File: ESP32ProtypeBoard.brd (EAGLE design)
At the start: 78.7 x 54.6 mm, 89 parts, among them IC1 ACT4088US-T, IC2 SI4431BDY, J4 VCC_TERMINAL, Q4 BSS138, U1 3.3V, U2 ESP-WROOM-32

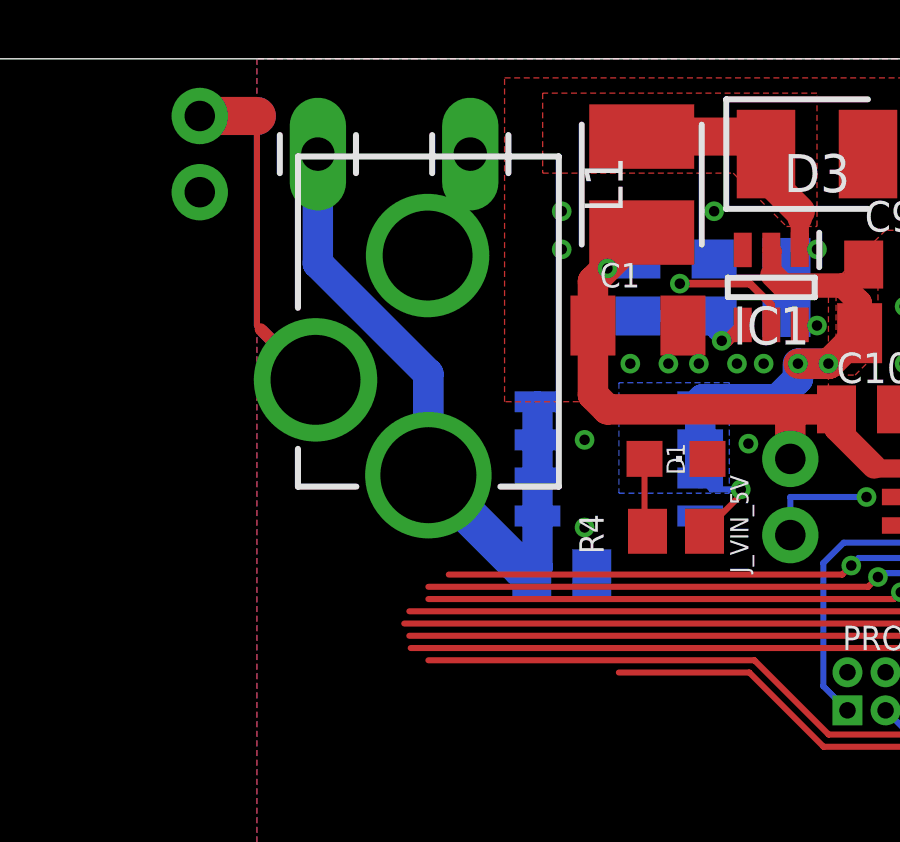
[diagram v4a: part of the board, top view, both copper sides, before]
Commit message: 12V pin
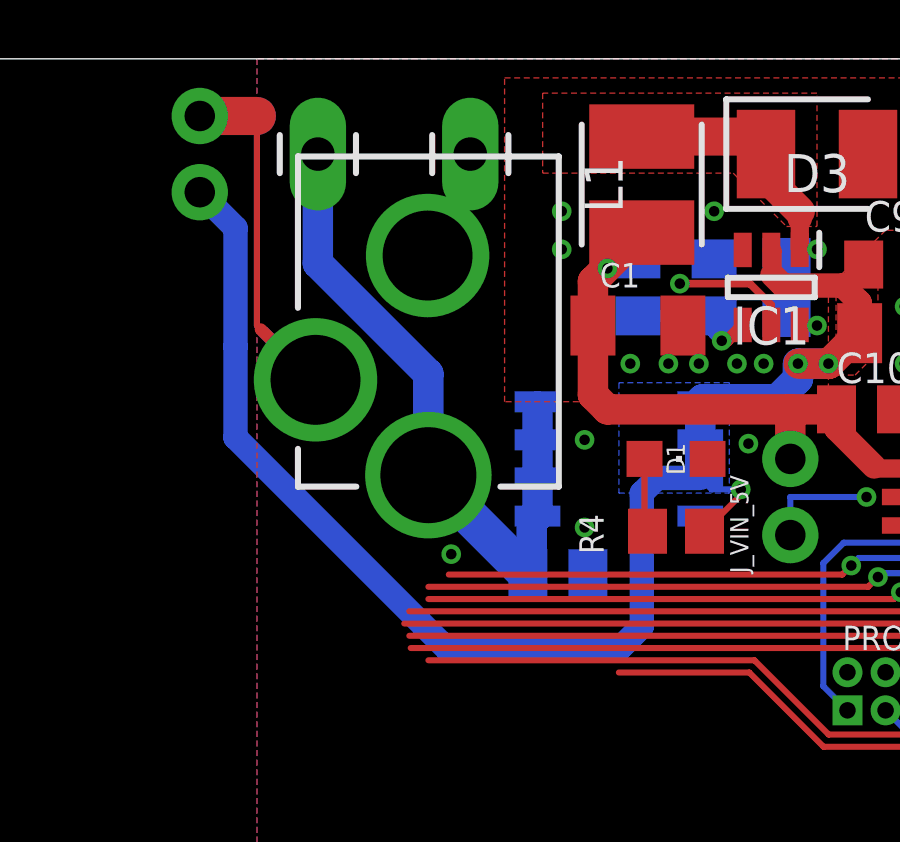
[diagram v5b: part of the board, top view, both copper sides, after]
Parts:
- moved C8 0.13 mm to (28.4, 37.5)
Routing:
- net +12V: track 18.6 -> 50.7 mm
- net GND: vias 31 -> 32
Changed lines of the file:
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@@
 <attribute name="VALUE" x="26.035" y="53.467" size="0.6096" layer="27" font="vector" ratio="20" rot="R180"/>
 </element>
-<element name="C8" library="rcl" library_urn="urn:adsk.eagle:library:334" package="C0805K" package3d_urn="urn:adsk.eagle:package:23681/2" value="0.1uF" x="28.575" y="37.465" smashed="yes" rot="MR180">
-<attribute name="NAME" x="29.21" y="38.735" size="0.8128" layer="26" rot="MR0"/>
-<attribute name="POPULARITY" value="52" x="28.575" y="37.465" size="1.778" layer="28" rot="MR180" display="off"/>
-<attribute name="SPICEPREFIX" value="C" x="28.575" y="37.465" size="1.778" layer="28" rot="MR180" display="off"/>
-<attribute name="VALUE" x="28.702" y="38.735" size="0.8128" layer="28" rot="MR0" align="bottom-center"/>
-<attribute name="VOLTAGE" value="25V" x="28.575" y="37.465" size="1.778" layer="28" rot="MR180" display="off"/>
+<element name="C8" library="rcl" library_urn="urn:adsk.eagle:library:334" package="C0805K" package3d_urn="urn:adsk.eagle:package:23681/2" value="0.1uF" x="28.448" y="37.465" smashed="yes" rot="MR180">
+<attribute name="NAME" x="29.083" y="38.735" size="0.8128" layer="26" rot="MR0"/>
+<attribute name="POPULARITY" value="52" x="28.448" y="37.465" size="1.778" layer="28" rot="MR180" display="off"/>
+<attribute name="SPICEPREFIX" value="C" x="28.448" y="37.465" size="1.778" layer="28" rot="MR180" display="off"/>
+<attribute name="VALUE" x="28.575" y="38.735" size="0.8128" layer="28" rot="MR0" align="bottom-center"/>
+<attribute name="VOLTAGE" value="25V" x="28.448" y="37.465" size="1.778" layer="28" rot="MR180" display="off"/>
 </element>
 <element name="J12" library="SparkFun-Connectors" library_urn="urn:adsk.eagle:library:513" package="1X11_NO_SILK" package3d_urn="urn:adsk.eagle:package:38260/1" value="" x="86.995" y="9.525" smashed="yes" rot="MR180">
@@
 <wire x1="36.195" y1="38.735" x2="36.195" y2="40.005" width="0.2032" layer="16"/>
 <wire x1="36.195" y1="40.005" x2="38.735" y2="40.005" width="0.2032" layer="16"/>
+<via x="24.892" y="38.1" extent="1-16" drill="0.35"/>
 <wire x1="125.095" y1="27.305" x2="130.175" y2="42.799" width="0" layer="19" extent="1-1"/>
 <wire x1="104.14" y1="29.21" x2="125.095" y2="27.305" width="0" layer="19" extent="1-1"/>
@@
 <wire x1="34.544" y1="40.259" x2="33.573" y2="40.259" width="0.2032" layer="16"/>
 <wire x1="33.573" y1="40.259" x2="33.192" y2="40.64" width="0.2032" layer="16"/>
-<wire x1="33.192" y1="43.18" x2="16.51" y2="50.165" width="0" layer="19" extent="16-16"/>
-<wire x1="36.4734" y1="44.45" x2="36.449" y2="44.45" width="0" layer="19" extent="1-1"/>
+<wire x1="33.192" y1="40.64" x2="31.75" y2="40.64" width="0.8128" layer="16"/>
+<wire x1="31.75" y1="40.64" x2="31.242" y2="40.132" width="0.8128" layer="16"/>
+<wire x1="31.242" y1="35.687" x2="30.48" y2="34.925" width="0.8128" layer="16"/>
+<wire x1="17.6996" y1="45.01545625" x2="17.702" y2="45.01785625" width="0.8128" layer="16"/>
+<wire x1="17.6996" y1="41.9904" x2="17.6996" y2="45.01545625" width="0.8128" layer="16"/>
+<wire x1="17.702" y1="48.973" x2="16.51" y2="50.165" width="0.8128" layer="16"/>
+<wire x1="31.242" y1="40.132" x2="31.242" y2="35.687" width="0.8128" layer="16"/>
+<wire x1="30.48" y1="34.925" x2="24.765" y2="34.925" width="0.8128" layer="16"/>
+<wire x1="24.765" y1="34.925" x2="17.6996" y2="41.9904" width="0.8128" layer="16"/>
+<wire x1="17.702" y1="45.01785625" x2="17.702" y2="48.973" width="0.8128" layer="16"/>
+<wire x1="36.449" y1="44.45" x2="36.4734" y2="44.45" width="0" layer="19" extent="1-1"/>
 </signal>
 <signal name="+5V">
@@
 <wire x1="20.4452" y1="47.7944625" x2="24.13" y2="44.1096625" width="1.016" layer="16"/>
 <wire x1="24.13" y1="40.7322" x2="27.2702" y2="37.592" width="1.27" layer="16"/>
-<wire x1="27.448" y1="37.592" x2="27.575" y2="37.465" width="1.27" layer="16"/>
-<wire x1="27.448" y1="37.592" x2="27.2702" y2="37.592" width="1.27" layer="16"/>
 <wire x1="27.768" y1="42.799" x2="27.768" y2="43.18" width="0.7112" layer="16"/>
 <wire x1="27.768" y1="41.91" x2="27.768" y2="40.64" width="1.016" layer="16"/>
 <wire x1="27.768" y1="40.64" x2="27.768" y2="39.37" width="1.016" layer="16"/>
-<wire x1="27.768" y1="39.37" x2="27.768" y2="37.658" width="1.016" layer="16"/>
-<wire x1="27.768" y1="37.658" x2="27.575" y2="37.465" width="1.016" layer="16"/>
 <wire x1="27.768" y1="41.91" x2="27.768" y2="42.799" width="1.016" layer="16"/>
+<wire x1="27.575" y1="39.177" x2="27.575" y2="37.592" width="1.016" layer="16"/>
+<wire x1="27.448" y1="37.465" x2="27.575" y2="37.592" width="1.016" layer="16"/>
+<wire x1="27.575" y1="39.177" x2="27.768" y2="39.37" width="1.016" layer="16"/>
+<wire x1="27.448" y1="37.465" x2="27.2702" y2="37.592" width="0" layer="19" extent="16-16"/>
 </signal>
 <signal name="D2A">

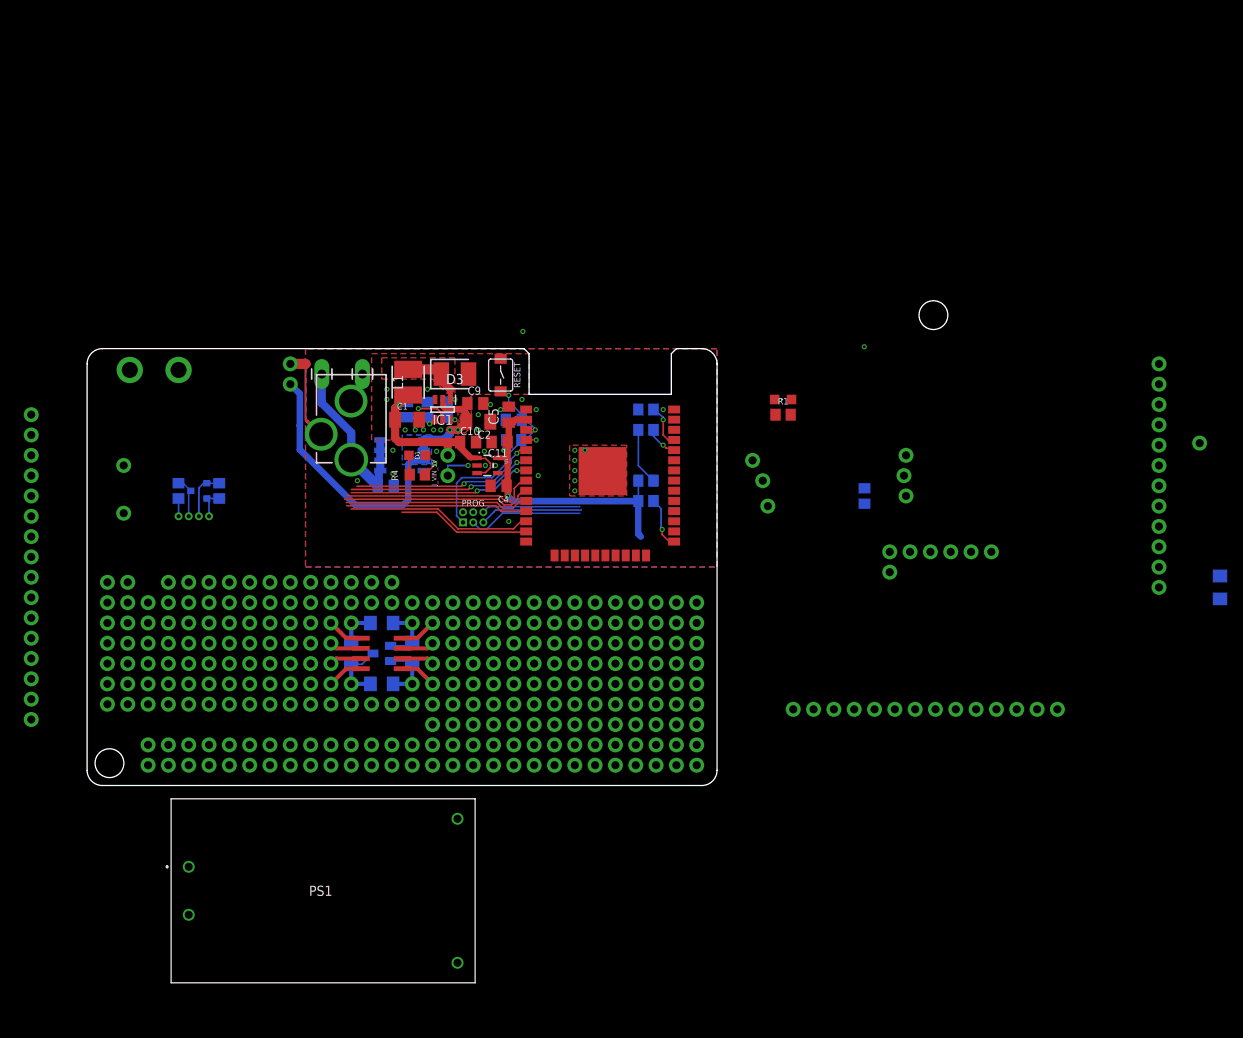
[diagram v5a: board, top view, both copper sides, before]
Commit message: first data lines, added new VIN pin closer
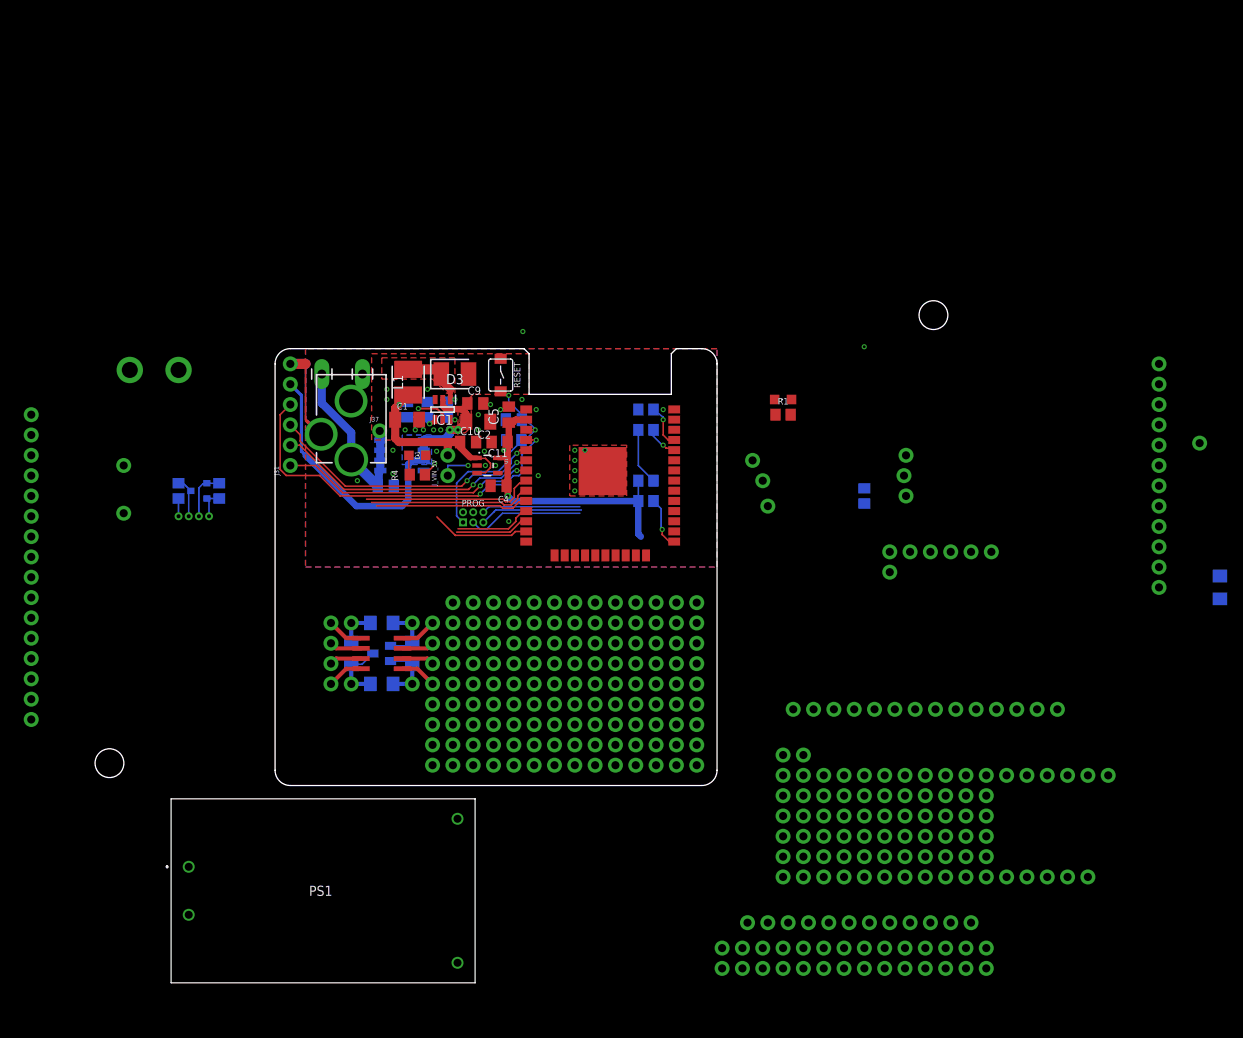
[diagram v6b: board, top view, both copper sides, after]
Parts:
- added J31: (no value), SparkFun-Connectors:1X04_NO_SILK
- added J37: (no value), SparkFun-Connectors:1X01NS_KIT
- moved J1 87.2 mm to (78.1, -8.89)
- moved J13 87.2 mm to (78.1, -1.27)
- moved J29 87.2 mm to (78.1, 3.81)
- moved J36 87.2 mm to (78.1, -6.35)
- moved J5 87.2 mm to (78.1, 1.27)
- moved J56 87.2 mm to (78.1, -3.81)
- moved J9 87.2 mm to (78.1, -11.4)
- moved J8 84.0 mm to (101.6, -17.1)
- moved J15 76.1 mm to (70.5, -20.3)
- moved J16 76.1 mm to (70.5, -22.9)
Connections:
- net IO34: now also J31.2
- net IO35: now also J31.1
- net IO36: now also J31.4
- net IO39: now also J31.3
- net VCC: now also J37.1
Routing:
- net IO36: track 1.26 -> 47.5 mm, vias 1 -> 2
- net IO27: track 23.3 -> 9.25 mm
- net IO26: track 22.8 -> 9.75 mm
- net IO39: track 23.4 -> 35.3 mm
- net IO34: track 23.4 -> 33.3 mm
- net IO35: track 23.0 -> 32.0 mm
- net IO14: track 16.6 -> 12.3 mm
- net IO25: track 23.2 -> 19.2 mm
- net IO33: track 23.9 -> 20.4 mm
- net IO32: track 24.6 -> 21.8 mm
- net VCC: track 22.5 -> 24.1 mm
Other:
- board size 78.7 x 54.6 mm -> 55.2 x 54.6 mm

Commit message: rerouted EN to bottom
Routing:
- net EN: track 26.8 -> 33.0 mm, vias 2 -> 3
- net GND: vias 32 -> 31
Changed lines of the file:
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@@
 <layer number="13" name="Route13" color="4" fill="5" visible="no" active="yes"/>
 <layer number="14" name="Route14" color="1" fill="6" visible="no" active="yes"/>
-<layer number="15" name="Route15" color="4" fill="6" visible="no" active="yes"/>
+<layer number="15" name="Route15" color="4" fill="6" visible="yes" active="yes"/>
 <layer number="16" name="Bottom" color="1" fill="1" visible="yes" active="yes"/>
 <layer number="17" name="Pads" color="2" fill="1" visible="yes" active="yes"/>
@@
 <via x="45.466" y="48.26" extent="1-16" drill="0.35"/>
 <via x="47.244" y="46.99" extent="1-16" drill="0.35"/>
-<via x="43.815" y="33.02" extent="1-16" drill="0.35"/>
-<via x="47.498" y="38.735" extent="1-16" drill="0.35"/>
+<via x="47.752" y="38.735" extent="1-16" drill="0.35"/>
 <via x="32.131" y="44.45" extent="1-16" drill="0.35"/>
 <via x="28.575" y="49.53" extent="1-16" drill="0.35"/>
@@
 <wire x1="47.117" y1="44.45" x2="45.847" y2="43.18" width="0.2032" layer="16"/>
 <wire x1="45.847" y1="43.18" x2="45.4" y2="43.18" width="0.2032" layer="16"/>
-<wire x1="37.2934" y1="33.6996" x2="37.2934" y2="37.8014" width="0.2032" layer="16"/>
-<wire x1="38.1" y1="32.893" x2="37.2934" y2="33.6996" width="0.2032" layer="16"/>
-<wire x1="37.2934" y1="37.8014" x2="38.735" y2="39.243" width="0.2032" layer="16"/>
-<wire x1="38.735" y1="39.243" x2="42.4757125" y2="39.243" width="0.2032" layer="16"/>
-<wire x1="43.71685625" y1="40.48414375" x2="42.4757125" y2="39.243" width="0.2032" layer="16"/>
-<wire x1="45.4" y1="43.18" x2="45.4" y2="43.053" width="0.2032" layer="16"/>
-<wire x1="43.71685625" y1="41.36985625" x2="43.71685625" y2="40.48414375" width="0.2032" layer="16"/>
-<wire x1="45.4" y1="43.053" x2="43.71685625" y2="41.36985625" width="0.2032" layer="16"/>
+<wire x1="38.1" y1="32.893" x2="38.22929375" y2="32.893" width="0.2032" layer="16"/>
+<wire x1="38.22929375" y1="32.893" x2="39.44409375" y2="31.6782" width="0.2032" layer="16"/>
+<wire x1="41.2724875" y1="31.6782" x2="39.44409375" y2="31.6782" width="0.2032" layer="16"/>
+<via x="47.371" y="33.274" extent="1-16" drill="0.35"/>
+<wire x1="47.371" y1="33.274" x2="42.8682875" y2="33.274" width="0.2032" layer="16"/>
+<wire x1="42.8682875" y1="33.274" x2="41.2724875" y2="31.6782" width="0.2032" layer="16"/>
+<wire x1="47.371" y1="33.274" x2="47.0516" y2="33.5934" width="0.2032" layer="1"/>
+<wire x1="47.0436" y1="41.29" x2="47.0516" y2="41.282" width="0.2032" layer="1"/>
+<wire x1="47.0436" y1="41.29" x2="47.0516" y2="41.298" width="0.2032" layer="1"/>
+<wire x1="47.878" y1="42.9173875" x2="47.878" y2="43.689" width="0.2032" layer="1"/>
+<wire x1="47.0516" y1="42.0909875" x2="47.878" y2="42.9173875" width="0.2032" layer="1"/>
+<wire x1="47.0516" y1="41.298" x2="47.0516" y2="42.0909875" width="0.2032" layer="1"/>
+<wire x1="47.878" y1="43.689" x2="47.117" y2="44.45" width="0.2032" layer="1"/>
+<wire x1="47.0516" y1="41.282" x2="47.0516" y2="33.5934" width="0.2032" layer="1"/>
 <wire x1="47.117" y1="44.45" x2="74.295" y2="40.64" width="0" layer="19" extent="1-1"/>
 </signal>
